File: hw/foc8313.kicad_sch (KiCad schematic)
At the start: 75 parts, among them J1 Tag Connect, J2 Encoder, J3 CAN, J4 CAN, J6 GPIO, SW1 SW_SPST, SW2 SW_SPST, U1 LMR36015SFBRNXR, U2 XC6206P332MR, U3 DRV8313PWP, U4 AS5047D, U4 STM32F103CBTx, U6 ZD24C08AE1-STGMT, X1 X322516MLB4SI

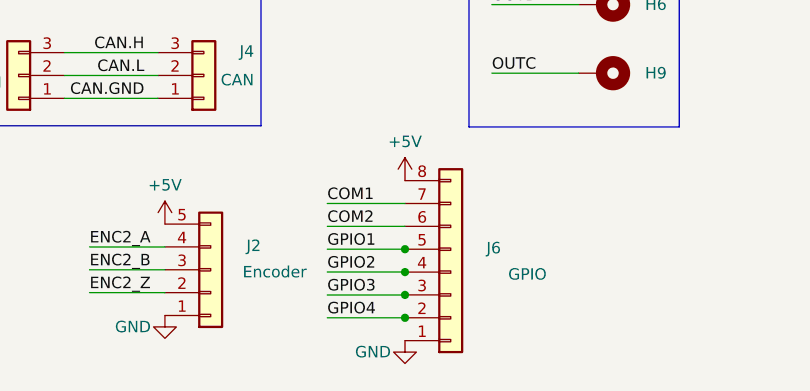
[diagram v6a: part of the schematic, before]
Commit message: [Hw] Added labels to silkscreen
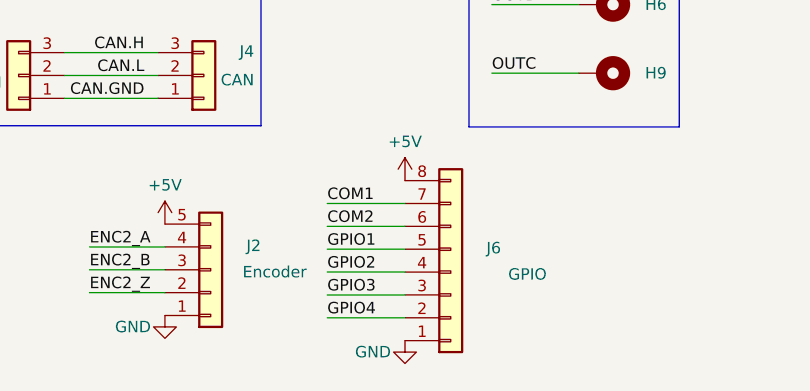
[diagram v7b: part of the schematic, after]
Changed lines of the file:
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@@
   (junction (at 70.485 58.42) (diameter 0) (color 0 0 0 0)
   )
-  (junction (at 143.764 209.55) (diameter 0) (color 0 0 0 0)
-  )
   (junction (at 197.866 157.734) (diameter 0) (color 0 0 0 0)
   )
@@
   (junction (at 188.722 26.67) (diameter 0) (color 0 0 0 0)
   )
-  (junction (at 143.764 217.17) (diameter 0) (color 0 0 0 0)
-  )
   (junction (at 129.032 167.894) (diameter 0) (color 0 0 0 0)
   )
@@
   (junction (at 60.452 58.42) (diameter 0) (color 0 0 0 0)
   )
-  (junction (at 143.764 214.63) (diameter 0) (color 0 0 0 0)
-  )
   (junction (at 92.71 58.42) (diameter 0) (color 0 0 0 0)
   )
@@
   )
   (junction (at 66.548 83.82) (diameter 0) (color 0 0 0 0)
-  )
-  (junction (at 143.764 212.09) (diameter 0) (color 0 0 0 0)
   )
   (junction (at 92.71 52.07) (diameter 0) (color 0 0 0 0)
@@
     (stroke (width 0) (type default))
   )
-  (wire (pts (xy 143.764 217.17) (xy 144.018 217.17))
-    (stroke (width 0) (type default))
-  )
   (wire (pts (xy 153.162 80.01) (xy 153.162 86.106))
     (stroke (width 0) (type default))
@@
     (stroke (width 0) (type default))
   )
-  (wire (pts (xy 143.764 214.63) (xy 144.018 214.63))
-    (stroke (width 0) (type default))
-  )
   (wire (pts (xy -54.356 191.262) (xy -54.356 186.436))
     (stroke (width 0) (type default))
@@
     (stroke (width 0) (type default))
   )
-  (wire (pts (xy 143.764 212.09) (xy 144.018 212.09))
-    (stroke (width 0) (type default))
-  )
   (wire (pts (xy -54.864 163.322) (xy -46.482 163.322))
     (stroke (width 0) (type default))
@@
     (stroke (width 0) (type default))
   )
-  (wire (pts (xy 143.764 209.55) (xy 144.018 209.55))
-    (stroke (width 0) (type default))
-  )
